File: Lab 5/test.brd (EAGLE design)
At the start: 100 x 80 mm, 48 parts, among them J1 FTDI_DEVICERA_SMT, M1 WIRELESS-NRF24L01, U1 3.3V, U2 GY-521MPU6050

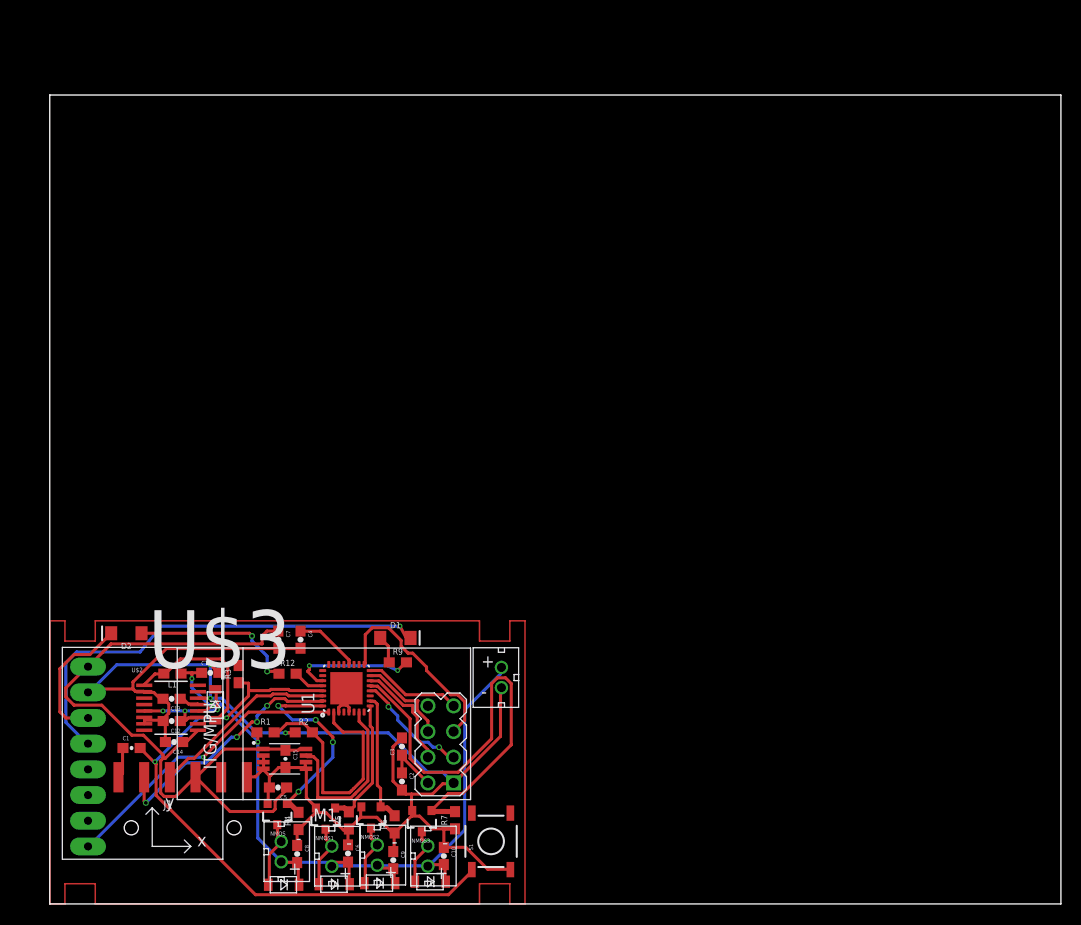
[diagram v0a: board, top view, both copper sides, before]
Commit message: Update template file, switch for the right Atmega MCU. Some advice from Arti:   - Everything need to be inside the board (all white frames inside): quadcopter propellers need clearance.   - Nothing under white frame except the Radio Module   - Battery JBT need to have +- on the edge of the PCB   - Mandatory: Top Polygon: VCC, Bottom Polygon: GND; Don't worry about Digital and Analog VCC and GND.
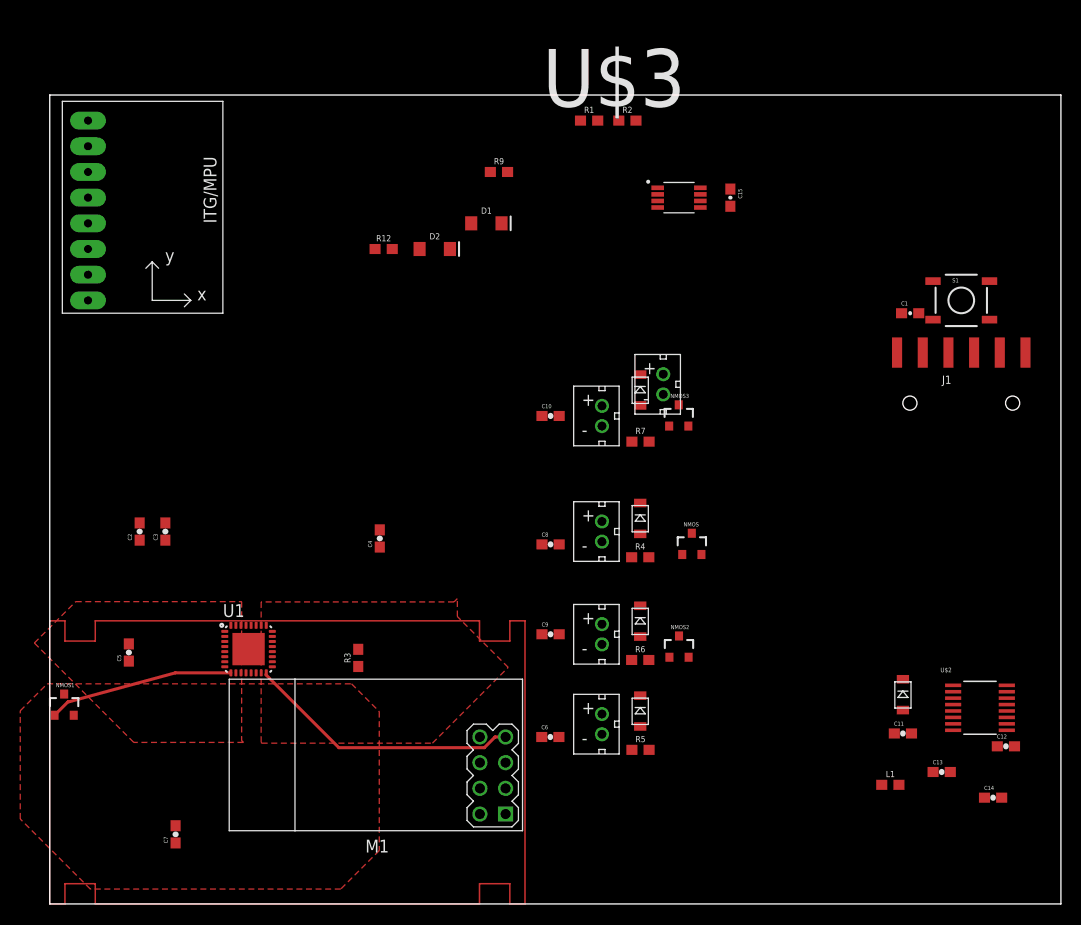
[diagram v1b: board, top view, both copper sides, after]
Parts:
- moved C1 88.2 mm to (85.1, 58.4)
- moved J1 87.7 mm to (90.1, 49.5)
- moved C12 82.5 mm to (94.6, 15.6), turned to 0 degrees
- moved C14 81.2 mm to (93.3, 10.5), turned to 0 degrees
- moved U$2 80.0 mm to (92.0, 19.4)
- moved C13 76.5 mm to (88.2, 13.1), turned to 0 degrees
- moved L1 71.8 mm to (83.1, 11.8), turned to 0 degrees
- moved S1 70.9 mm to (90.1, 59.7), turned to 0 degrees
- moved C15 70.8 mm to (67.3, 69.8)
- moved C11 68.8 mm to (84.4, 16.9)
- moved R1 68.4 mm to (53.3, 77.5)
- moved R2 68.4 mm to (57.1, 77.5)
- moved DIODE4 68.0 mm to (84.4, 20.7)
- moved U$3 67.8 mm to (62.2, 69.8)
- moved U2 54.0 mm to (12.7, 68.6)
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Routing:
- net GND: track 163.3 -> 0.00 mm, vias 3 -> 0
- net BATTERY+: track 80.0 -> 0.00 mm, vias 3 -> 0
- net VCC: track 79.4 -> 0.00 mm
- net RESET: track 63.5 -> 0.00 mm, vias 2 -> 0
- net MOTOR4: track 46.1 -> 0.00 mm
- net IMU-SDA: track 45.5 -> 0.00 mm, vias 1 -> 0
- net IMU-INT: track 29.3 -> 0.00 mm, vias 1 -> 0
- net FTDI-TX: track 25.0 -> 0.00 mm, vias 4 -> 0
- net MEASURE_PIN: track 24.5 -> 0.00 mm
- net MOTOR1: track 21.0 -> 0.00 mm, vias 4 -> 0
- net RF-SCK: track 20.1 -> 0.00 mm
- net FTDI-RX: track 18.6 -> 0.00 mm
- net OSC1: track 17.9 -> 0.00 mm
- net RF-MISO: track 9.71 -> 27.1 mm
- net N$9: track 16.4 -> 0.00 mm, vias 2 -> 0
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- added copper zone on layer 1, net VCC
